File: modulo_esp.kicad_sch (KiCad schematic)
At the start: 0 parts

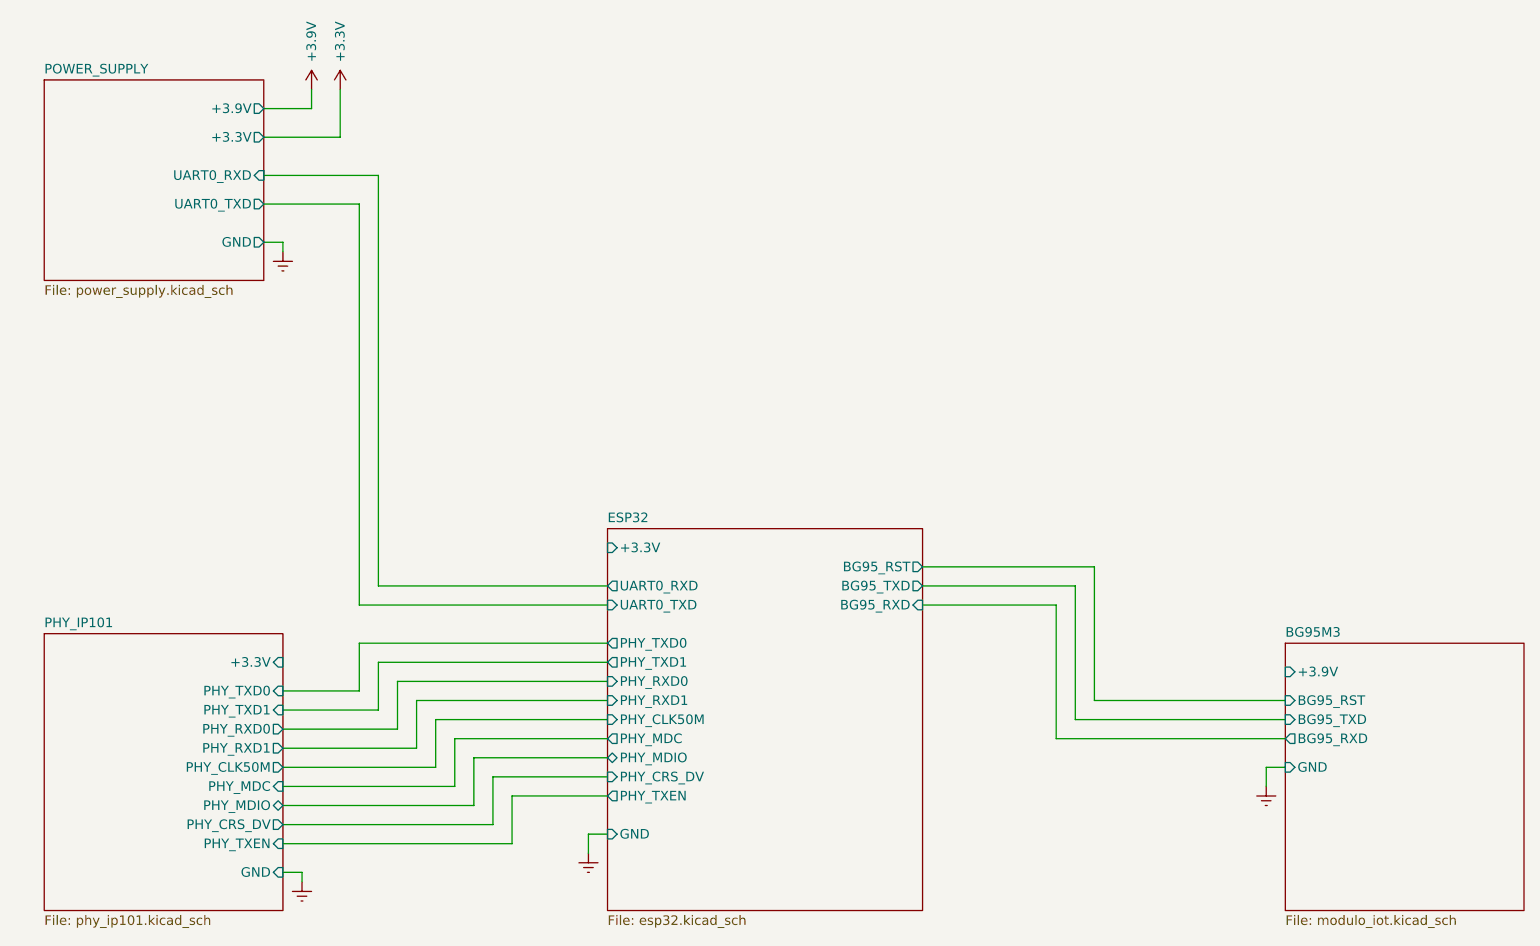
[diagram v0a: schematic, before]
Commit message: Inserido ferrite bead para cada sheet
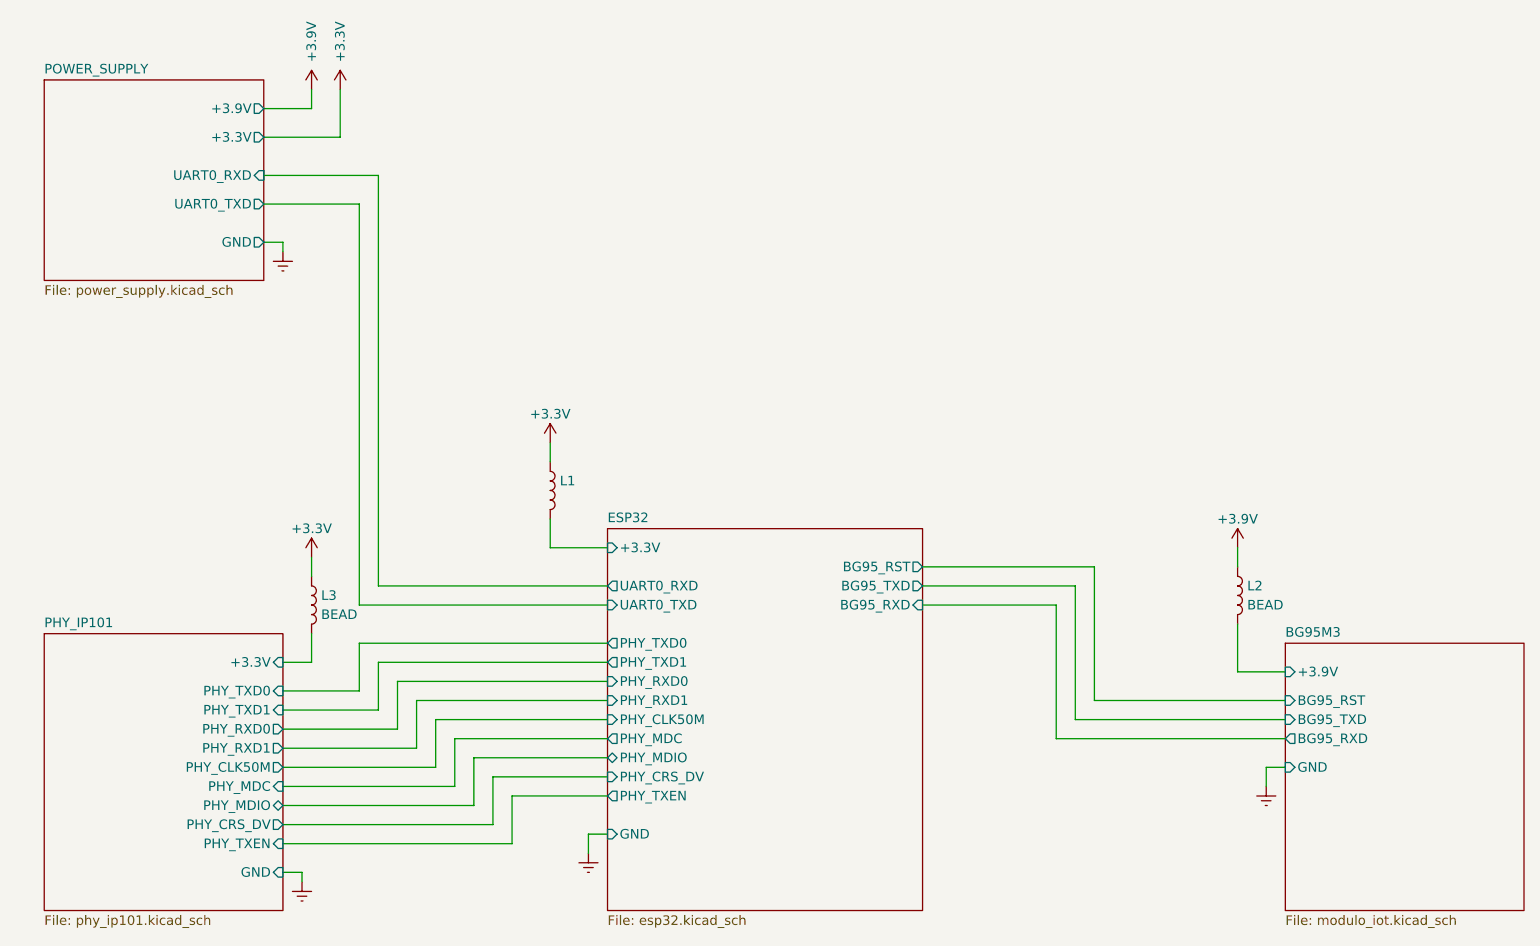
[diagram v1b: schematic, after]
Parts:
- added L1: (no value), symbol Device:L
- added L2, L3: BEAD, Inductor_SMD:L_0603_1608Metric_Pad1.05x0.95mm_HandSolder, symbol Device:L
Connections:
- net +3V3: now also L1.1, L3.1
- net BG95M3/+3.9V: now also L2.2
- net ESP32/+3.3V: now also L1.2
- net PHY_IP101/+3.3V: now also L3.2

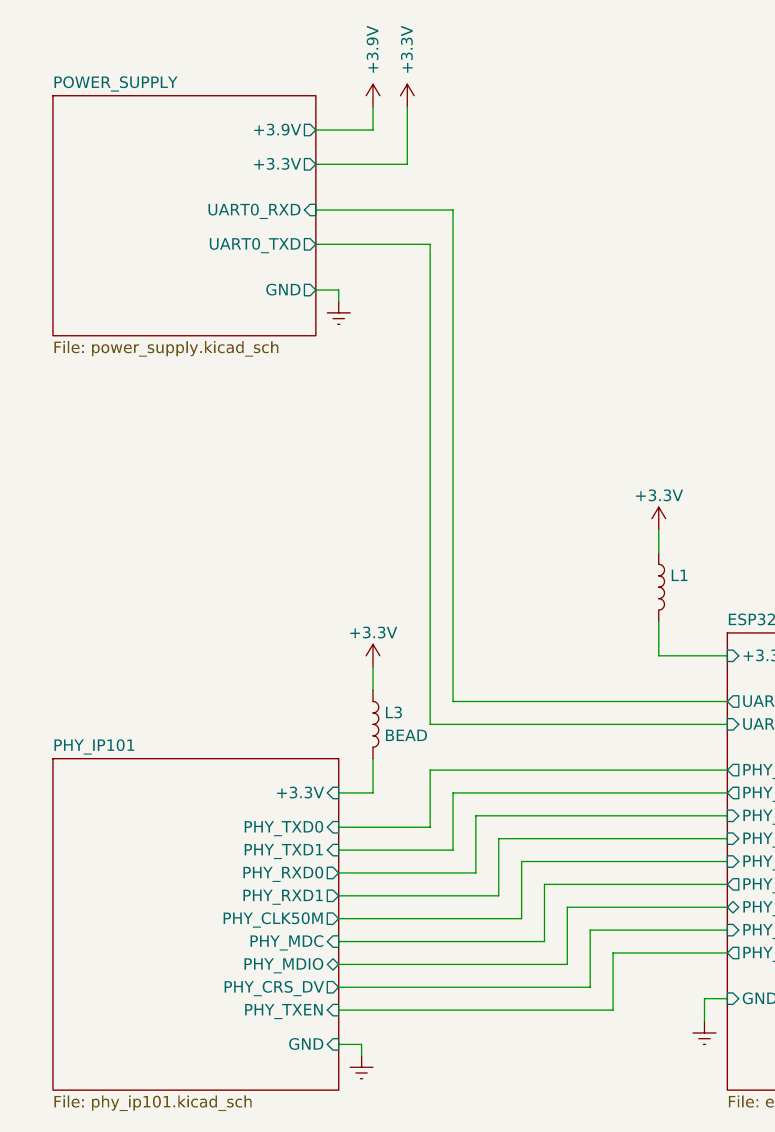
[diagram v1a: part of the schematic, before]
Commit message: Continuando a adição dos hierarchical labels
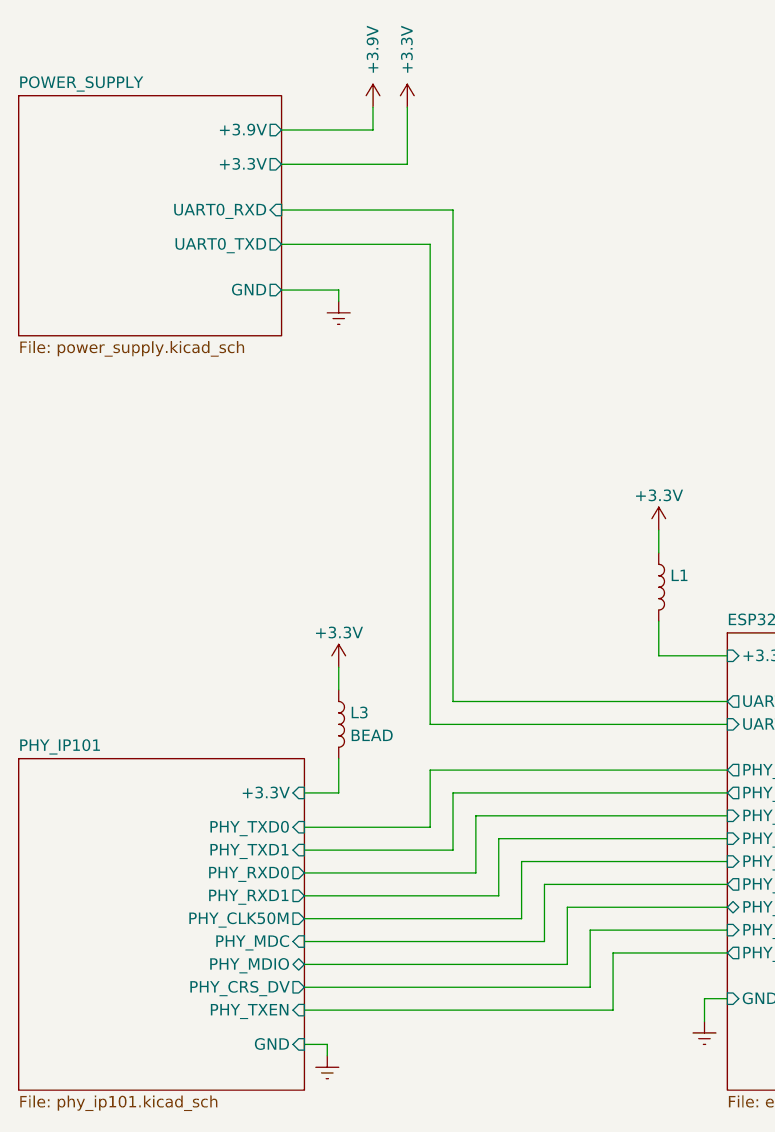
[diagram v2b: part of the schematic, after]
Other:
- moved on the sheet: L3

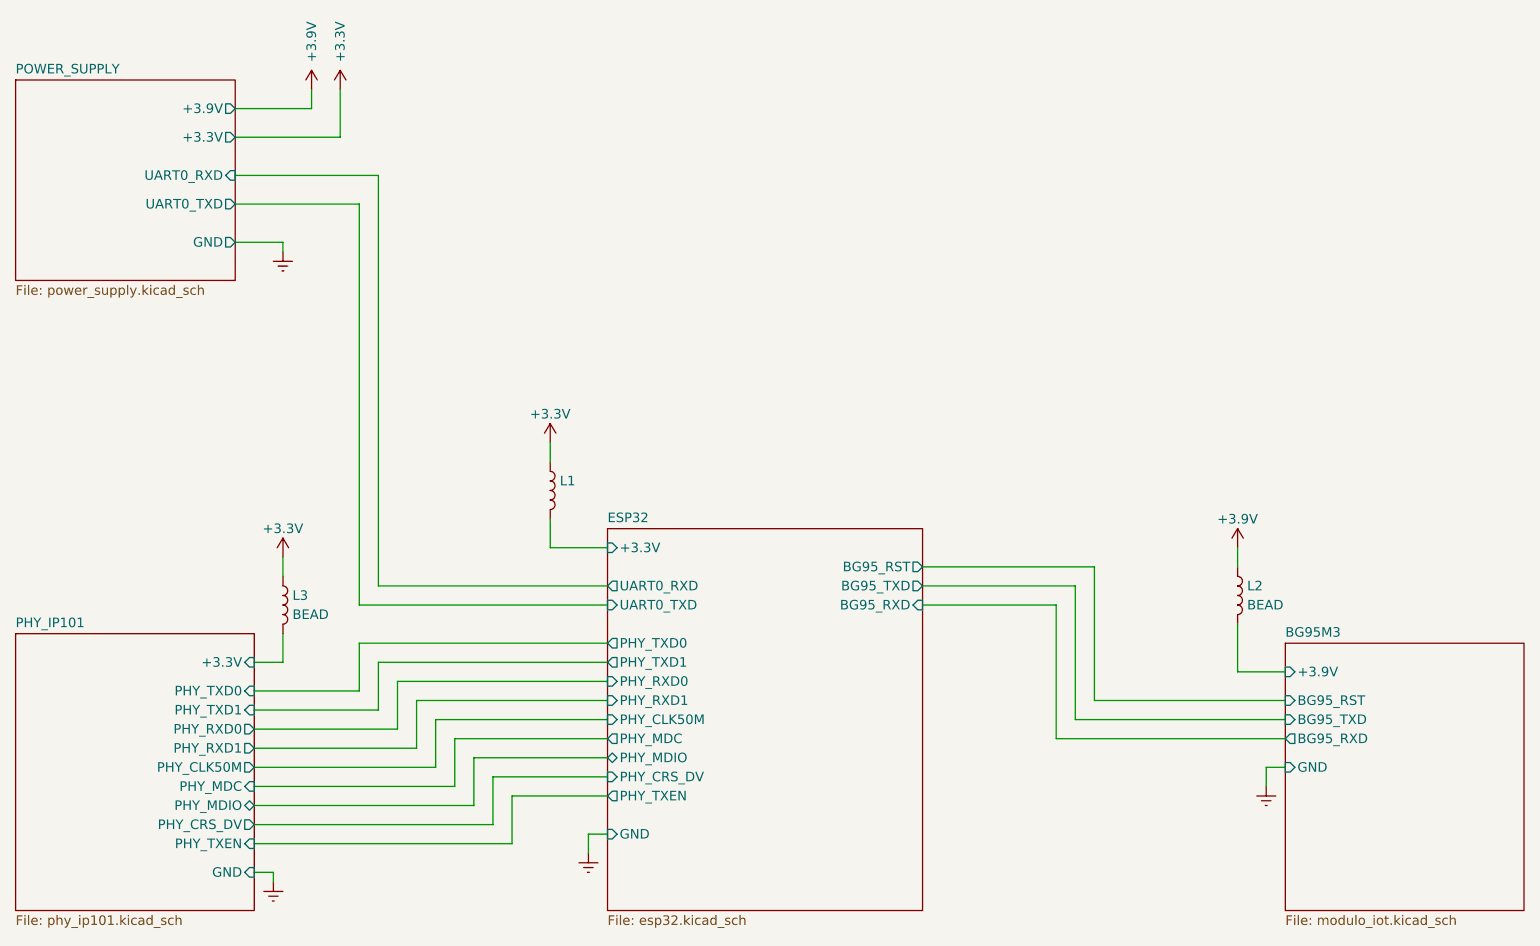
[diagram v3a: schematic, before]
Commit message: Corrigido alguns ERC e adicionado circuito DTR e RI do BG95
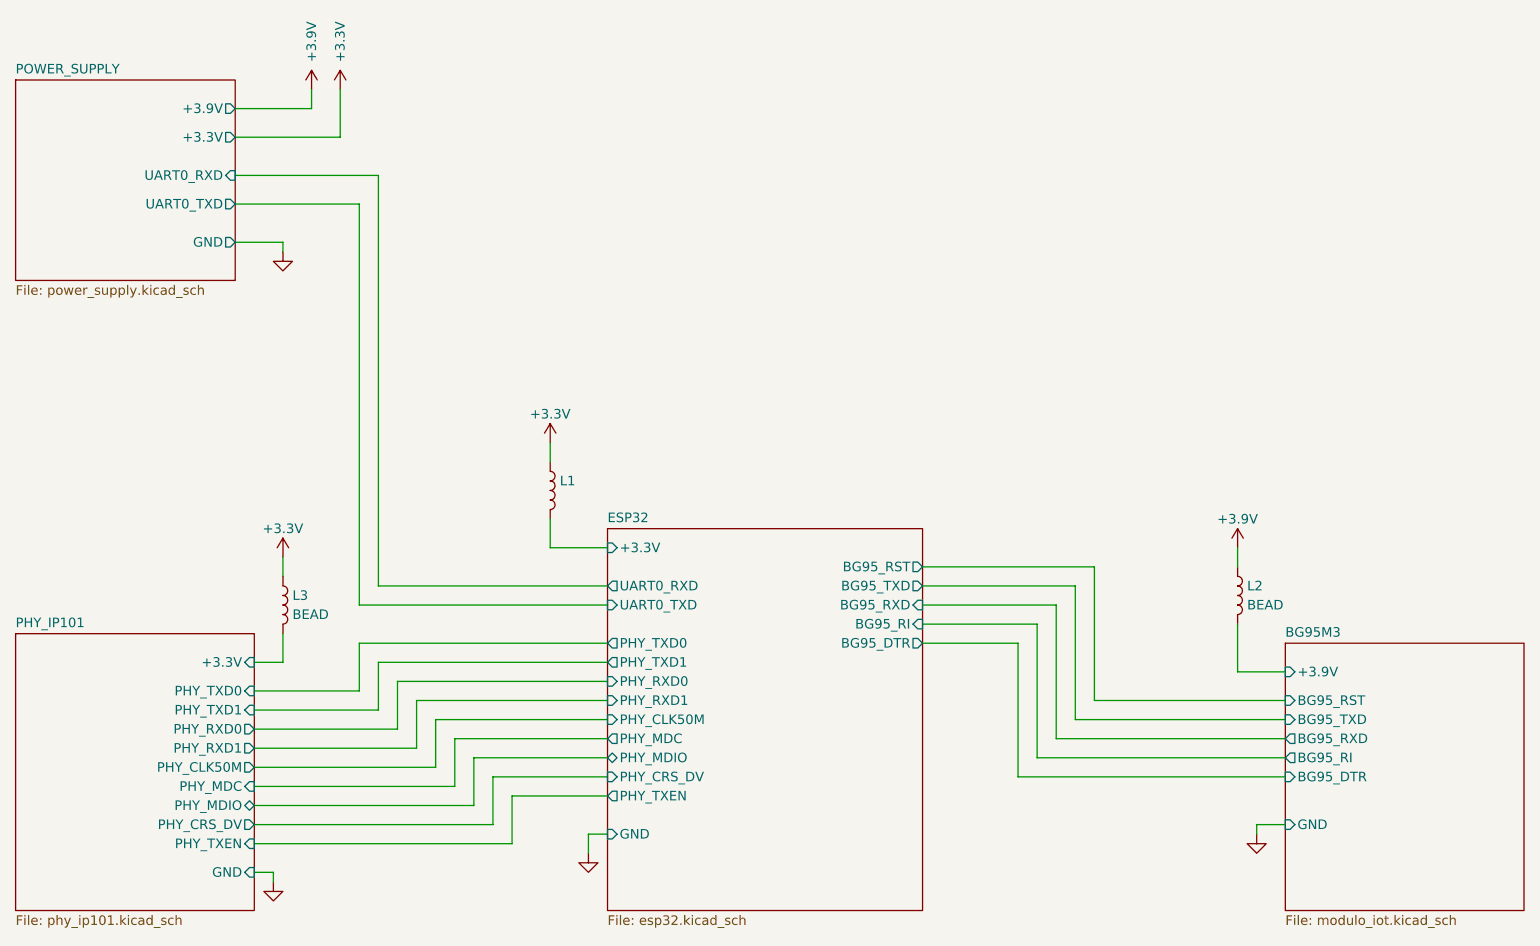
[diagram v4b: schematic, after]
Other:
- sheet BG95M3 ports: added BG95_DTR, BG95_RI; removed none
- sheet ESP32 ports: added BG95_DTR, BG95_RI; removed none

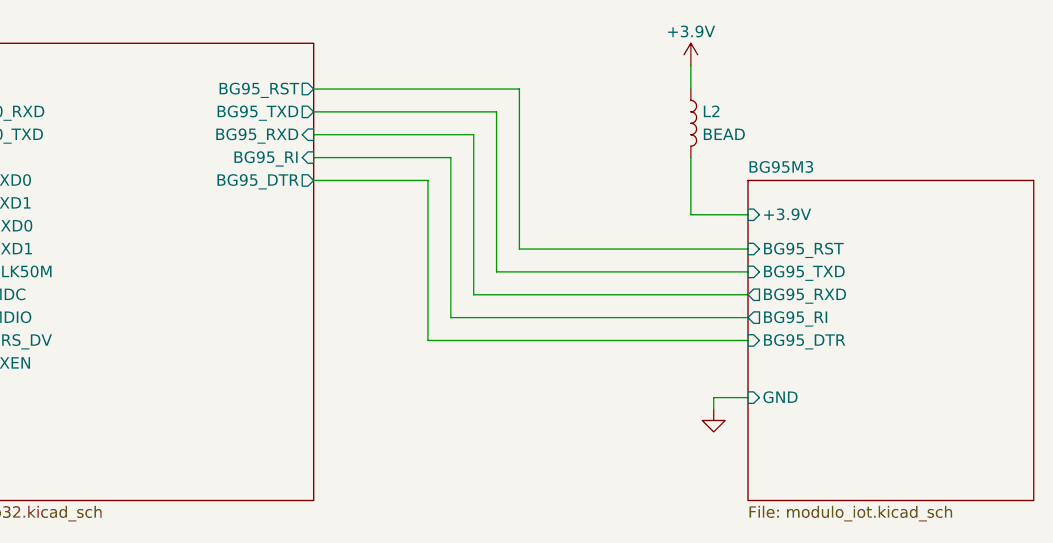
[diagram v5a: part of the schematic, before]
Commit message: Corrigido todos os ERC
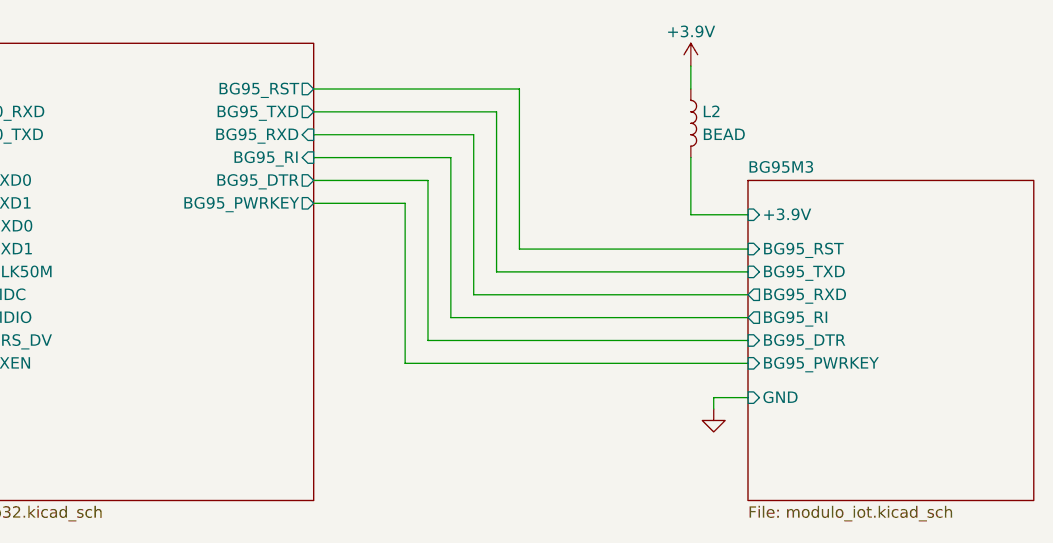
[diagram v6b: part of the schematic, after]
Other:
- sheet BG95M3 ports: added BG95_PWRKEY; removed none
- sheet ESP32 ports: added BG95_PWRKEY; removed none
